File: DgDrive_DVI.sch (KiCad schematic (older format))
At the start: 41 parts, among them J1 Curr. Mod., J2 DVI-I, J3 Ld+, J4 Ld-, J5 Pz+, J6 Pz-, J7 Piezo_In, K1 G6AU, Q1 MMBT3904, Q2 2N4401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

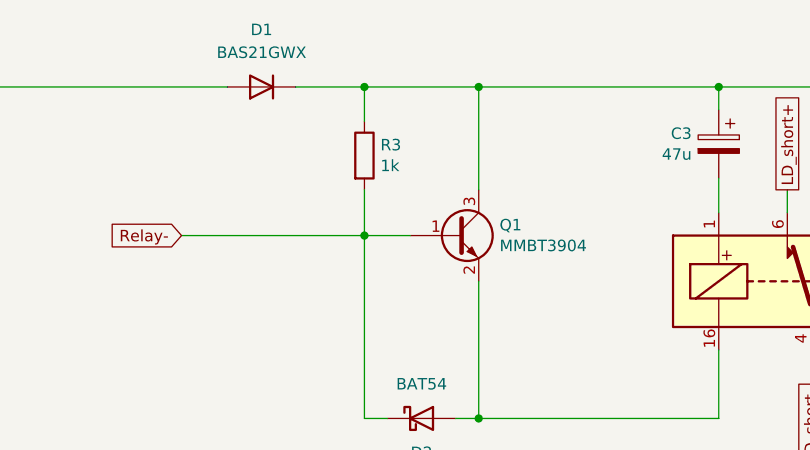
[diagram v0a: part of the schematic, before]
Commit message: R3=100k to reduce relay circuit idle current
This enables activating the laser using a 9V-battery.
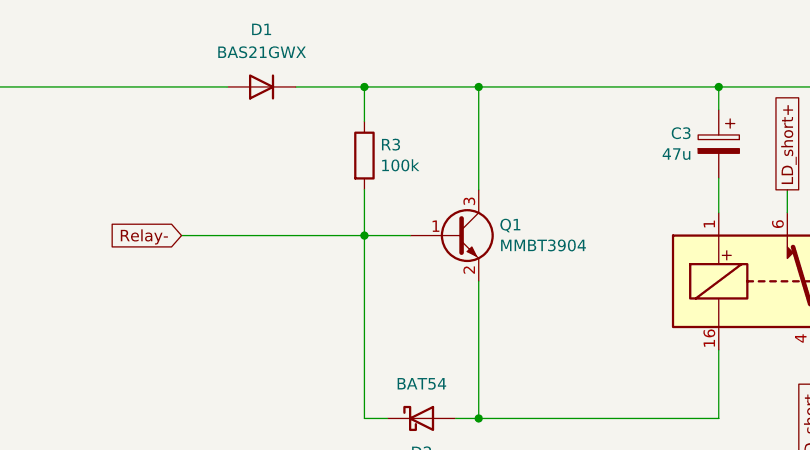
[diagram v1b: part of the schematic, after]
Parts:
- R3: value 1k -> 100k; PN RR0816P-102-D -> (none)
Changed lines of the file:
@@
 P 3350 1250
 F 0 "R3" H 3420 1296 50  0000 L CNN
-F 1 "1k" H 3420 1205 50  0000 L CNN
+F 1 "100k" H 3420 1205 50  0000 L CNN
 F 2 "Resistor_SMD:R_0603_1608Metric" V 3280 1250 50  0001 C CNN
 F 3 "" H 3350 1250 50  0001 C CNN
 F 4 "Susumu" H 3350 1250 60  0001 C CNN "MFN"
-F 5 "RR0816P-102-D" H 3350 1250 50  0001 C CNN "PN"
+F 5 "" H 3350 1250 50  0001 C CNN "PN"
 	1    3350 1250
 	1    0    0    -1

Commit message: SMD solder pads for piezo connection
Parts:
- J5, J6: footprint Connector_Wire:SolderWirePad_1x01_Drill1mm -> TestPoint:TestPoint_Keystone_5015_Micro-Minature
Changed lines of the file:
@@
 Sheet 1 1
 Title "Laser Backplane Diode DVI"
-Date "2021-10-07"
+Date "2021-11-02"
 Rev "1.6"
 Comp "APQ"
@@
 F 0 "J5" H 9068 925 50  0000 C CNN
 F 1 "Pz+" H 9068 1016 50  0000 C CNN
-F 2 "Connector_Wire:SolderWirePad_1x01_Drill1mm" H 9150 1150 50  0001 C CNN
+F 2 "TestPoint:TestPoint_Keystone_5015_Micro-Minature" H 9150 1150 50  0001 C CNN
 F 3 "~" H 9150 1150 50  0001 C CNN
 F 4 "DNF" H 9150 1150 50  0001 C CNN "Config"
@@
 F 0 "J6" H 9068 1275 50  0000 C CNN
 F 1 "Pz-" H 9068 1366 50  0000 C CNN
-F 2 "Connector_Wire:SolderWirePad_1x01_Drill1mm" H 9150 1500 50  0001 C CNN
+F 2 "TestPoint:TestPoint_Keystone_5015_Micro-Minature" H 9150 1500 50  0001 C CNN
 F 3 "~" H 9150 1500 50  0001 C CNN
 F 4 "DNF" H 9150 1500 50  0001 C CNN "Config"

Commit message: Current modulation: add input series resitance for proper roll-off and capacitance at Ld- for flat response.
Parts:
- added C5: DNF, Capacitor_SMD:C_0603_1608Metric, symbol Device:C_Small
- added C6: 10n, Capacitor_SMD:C_0603_1608Metric, symbol Device:C_Small
- added R6: 1k, Resistor_SMD:R_0603_1608Metric, symbol Device:R_Small
- added R9: 4.7, Resistor_SMD:R_0603_1608Metric, symbol Device:R_Small
- R3: PN (none) -> RR0816P-104-D
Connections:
- net GND: now also C5.1, C6.2
- net LD_short-: now also R9.1
- net at J1.1 (In), R2.1: now also R6.1; no longer U1.3 (+)
- net Ld+: now reaches J2.10 (D1+), J2.13 (D3+), L1.1, R1.2
- new net: C5.2, R6.2, U1.3 (+)
- new net: C6.1, R9.2
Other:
- note added: "Close JP2 for GND referenced laser current drivers. \nFor floating devices, C6 is used to provide a low\nimpedance node for the current modulation at \nhigh frequencies. R9 guarantees stability of the \ndriver under capactivte load."
- note added: "In combination with the input capacitance of U6A,\nR6 defines a proper roll-off above 100 MHz. \nUse C5 to add input capacitance."
- note added: "Q2 is used as reverse and over voltage protection"
- note added: "R1 absorbs reflections in the cable.\nL1 is used to by-pass R1 for the DC-current."
- note added: "R3 defines the idle current of the protection circuit."
- note added: "The R7 and R8 resistors are for protection."
- note removed: "The 1k resistors are for protection"
- moved on the sheet: C4, J1, J3, J4, JP2, L1, Q2, R1, R2, R4, R7, R8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
